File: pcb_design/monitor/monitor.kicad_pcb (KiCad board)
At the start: 2 copper layers, 12 parts

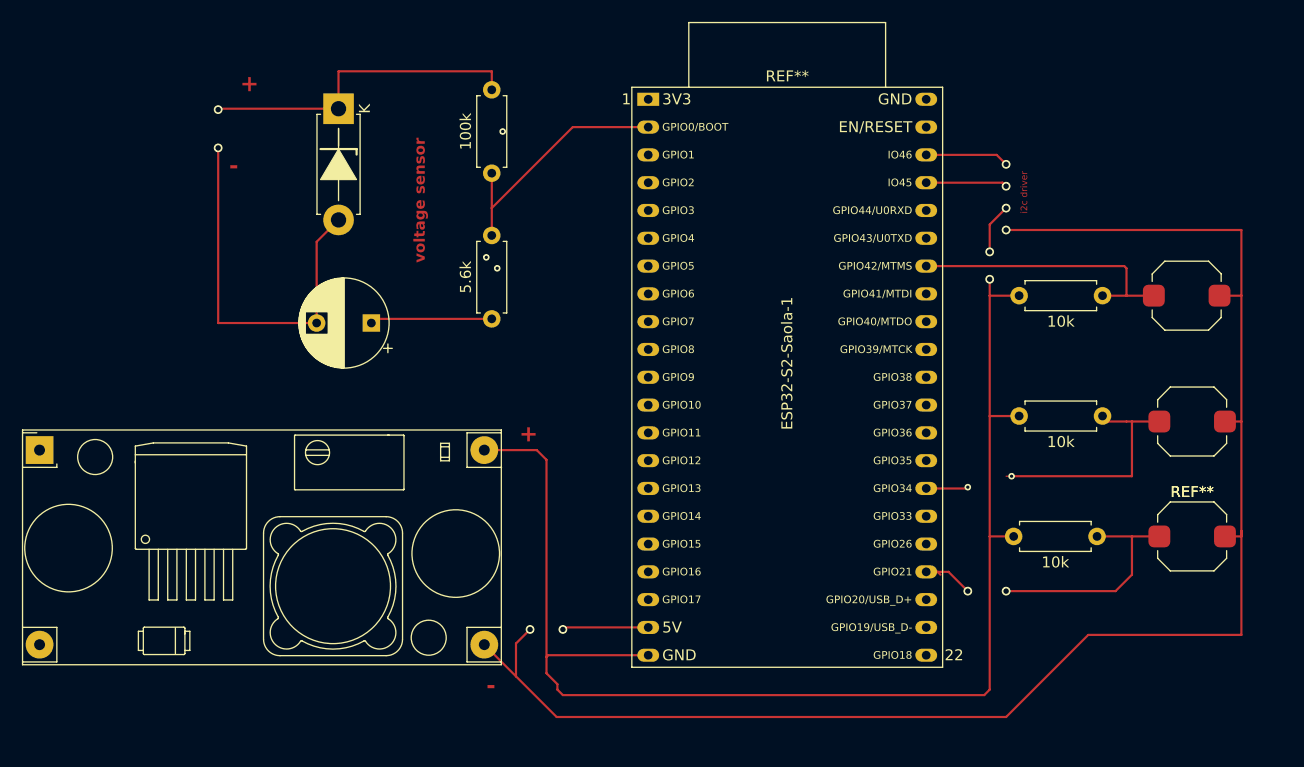
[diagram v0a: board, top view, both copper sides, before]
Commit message: Update fp-info-cache in switch design ``
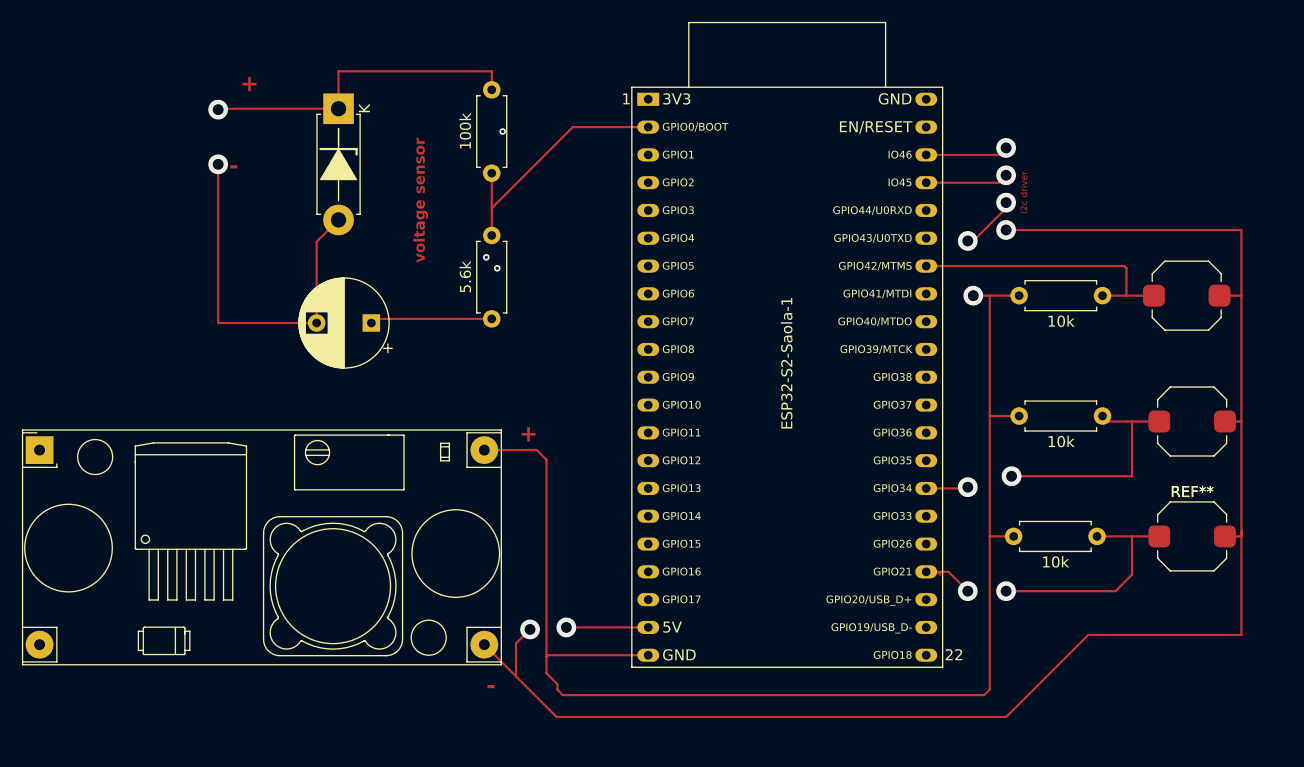
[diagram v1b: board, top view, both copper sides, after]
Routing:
- net (no net): track 471.0 -> 469.8 mm

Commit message: Refactor PCB design files and update switch design dependencies
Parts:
- removed the REF** at (108.3, 77.6)
- added REF**: ESP_Test, esp332:ESP_Test (1), F.Cu at (119.9, 111.0)
- moved REF** 9.51 mm to (158.0, 105.0)
- moved 10k 9.01 mm to (149.5, 104.5)
- moved REF** 9.00 mm to (158.0, 126.5)
- moved REF** 8.51 mm to (158.5, 115.5)
- moved 10k 7.53 mm to (150.0, 125.0)
- moved 10k 5.51 mm to (149.5, 112.0)
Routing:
- net (no net): track 469.8 -> 513.8 mm, vias 18 -> 19
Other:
- board outline added: 26 x 49 mm
